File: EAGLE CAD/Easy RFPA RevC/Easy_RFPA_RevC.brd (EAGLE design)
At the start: 127 x 147.3 mm, 296 parts, among them IC1 LM741D, IC2 LM741D, IC3 LM393D, IC5 74AHC1G00DBV, IC6 74LS74D, IC7 74AHC1G86DBV, J401 HDR_2X1282836-1282836-1, J402 KK_PCFAN, Q1 IRF630, Q101 IRF520N, Q102 IRF630, Q2 MOSFET_NBSS123SOT23, Q201 IRF630, Q202 IRF630, Q3 NPNMMBT3904SOT23_BEC, Q301 MOSFET_NBSS123SOT23, Q302 PNPSOT23_BEC, Q303 NPNMMBT3904SOT23_BEC, Q4 PNPSOT23_BEC, Q5 IRF630, SW1 SPST_NO_TACT_RA43125608371643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, SW2 SPST_NO_TACT_RA43125608371643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, T1 HP1_TRAFO, T102 HP4_TRAFO, U1 OPAMP_QUADTLV274IDSOIC14, U2 ADJ_ZENERTL431AILPRAGTO-92-LP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, U302 OPAMP_QUADTLV274IDSOIC14, U401 LDO_3TERMMC78M12CTGTO220_VERT, U402 LDO_3TERMMC78M05CTGTO220_VERT, X1 1-227161-0, X2 1-227161-0, X4 1-227161-0, X402 HEATSINK_OMNI_DUALOMNI-UNI-30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

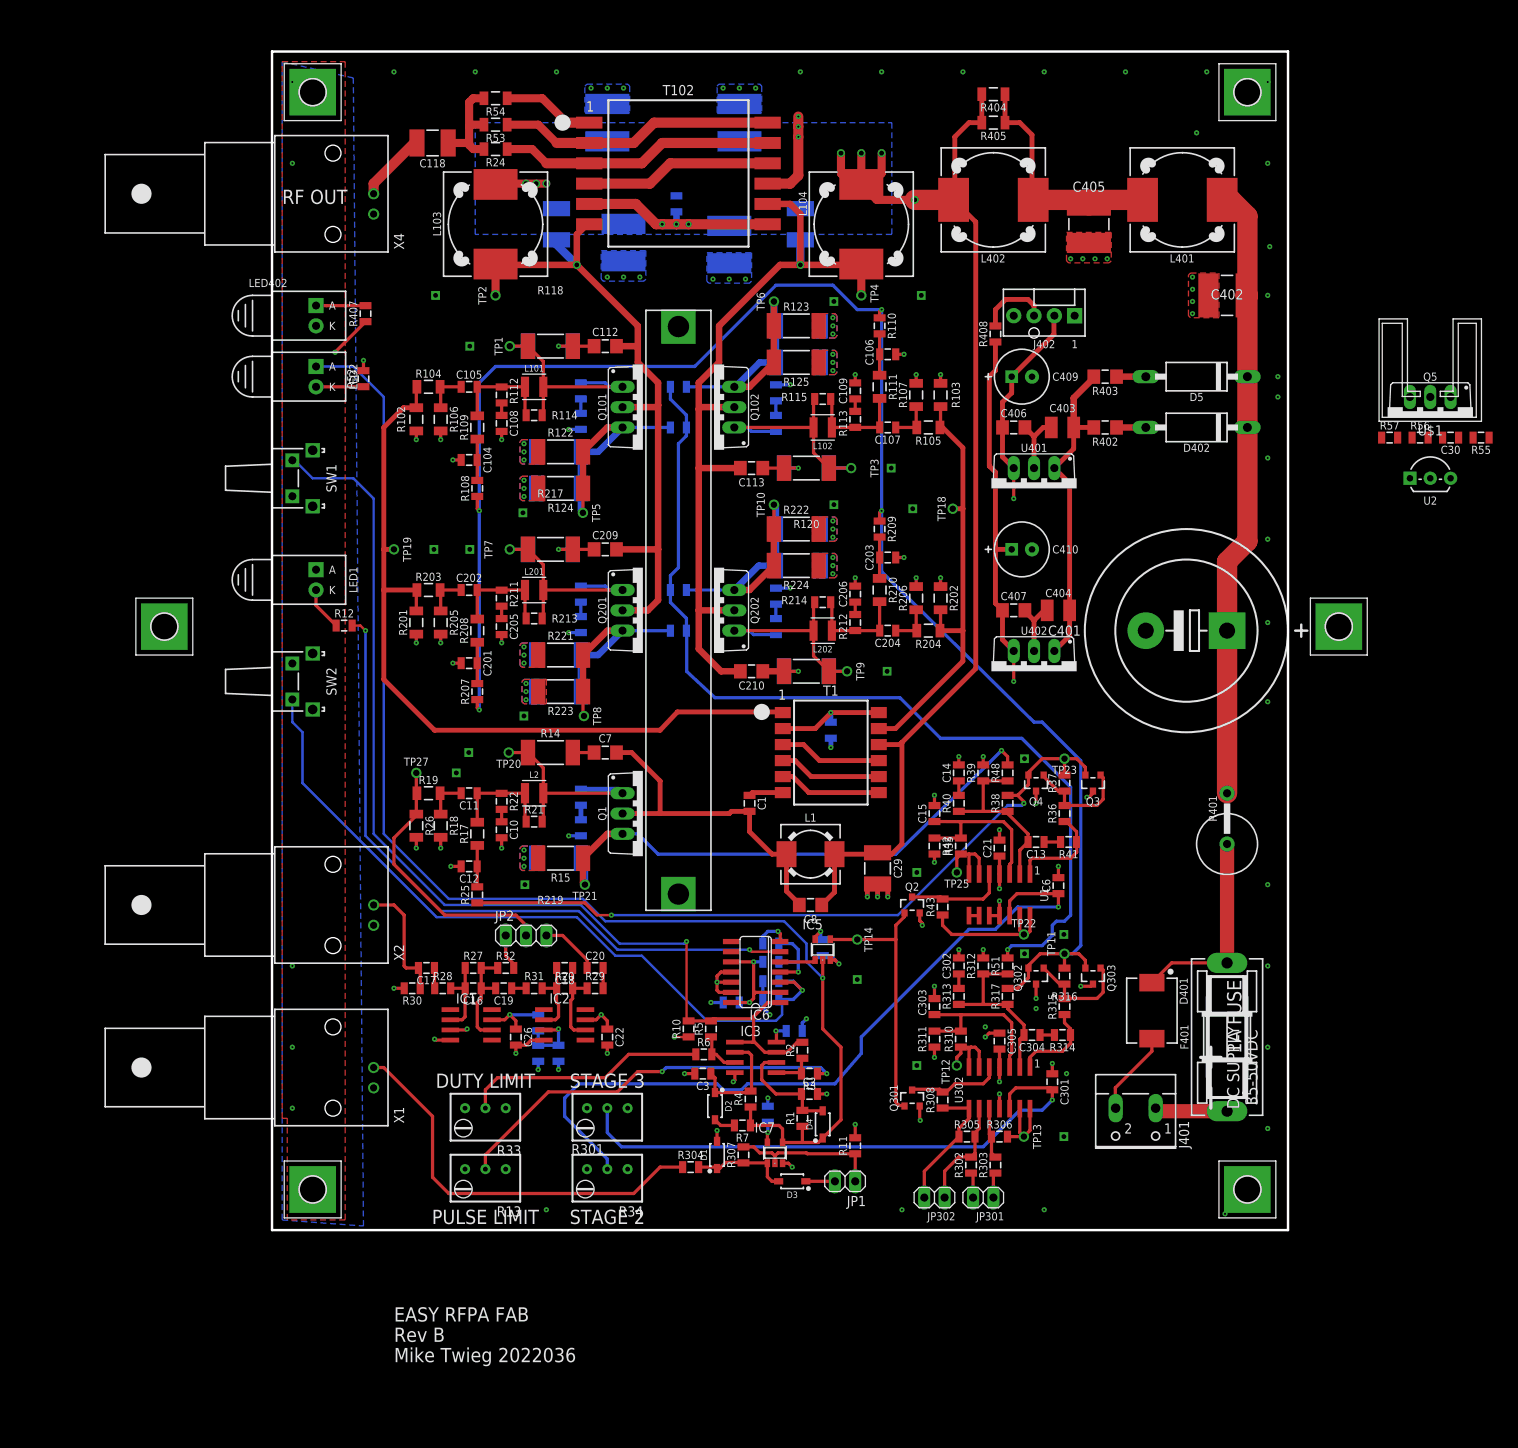
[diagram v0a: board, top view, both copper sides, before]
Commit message: Put discrete LDO on board
Remove old zeners
Move smaller electrolytic caps towards load circuitry to free up space
Move extra mounting holes onto board
Should consider reordering buttons/LEDs on west edge
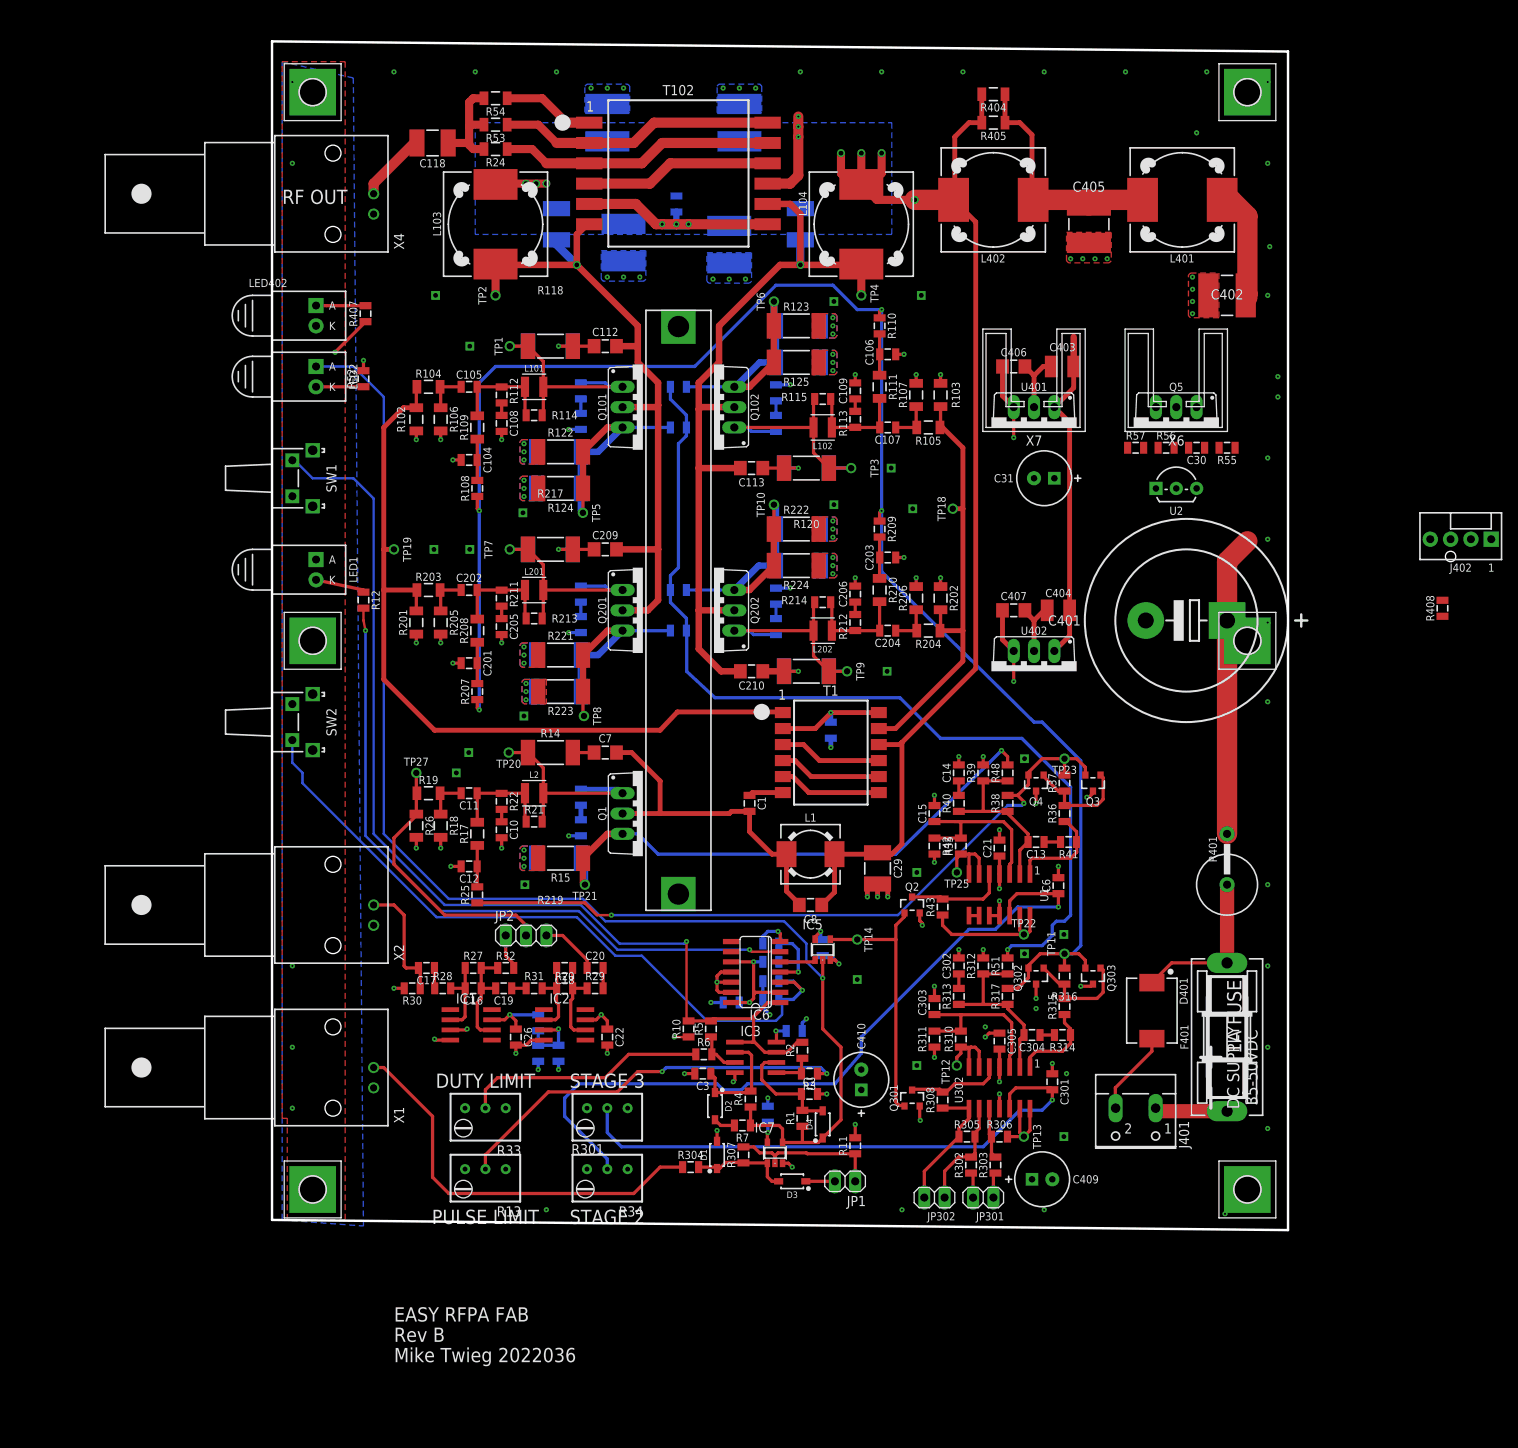
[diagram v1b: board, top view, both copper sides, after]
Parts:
- removed D402, D5: D-ZENER1N5355B-TPDO15-12, MDT_Diode:DO15-12
- removed R402, R403: 1.0, MDT_R:R1206
- removed U$1: (no value), MDT_HEATSINK:ATS-PCBT1085
- added C31: 22uF, MDT_C:E2,5-7
- added X6, X7: HEATSINK_CLIPONATS-PCBT1085ATS-PCBT1085, MDT_HEATSINK:ATS-PCBT1085
- moved C409 100.4 mm to (96.3, -1.27)
- moved C410 69.3 mm to (73.7, 11.2), turned to 90 degrees
- moved R408 65.6 mm to (146.3, 70.1)
- moved J402 59.1 mm to (148.6, 78.7)
- moved C30 31.8 mm to (115.6, 90.2)
- moved Q5 31.8 mm to (113.0, 92.7)
- moved R55 31.8 mm to (119.4, 90.2)
- moved U2 31.8 mm to (113.0, 85.1)
- moved R56 31.8 mm to (111.8, 90.2)
- moved R57 31.8 mm to (108.0, 90.2)
- moved H1 18.6 mm to (5.08, 66.0)
- moved H2 11.6 mm to (121.9, 66.0)
- moved C403 7.62 mm to (98.8, 100.3)
- moved C406 7.62 mm to (92.7, 100.3)
- moved U401 7.62 mm to (95.2, 92.7)
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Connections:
- removed net N$28: D5.A, R403.1
- removed net N$32: D402.A, R402.1
- net +24V: now also C31.+; no longer R402.2, R403.2
- net GND: now also C31.-
- net VB_ICL: no longer D402.C, D5.C
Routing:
- net VB_ICL: track 79.0 -> 52.0 mm
- net +5V: track 235.1 -> 208.4 mm
- net +12V: track 73.7 -> 61.8 mm
- net N$51: track 8.99 -> 0.00 mm
- net VB_FUSED: track 25.3 -> 20.2 mm
- net RESET: track 95.6 -> 90.5 mm
- net N$32: track 3.66 -> 0.00 mm
- net N$28: track 3.66 -> 0.00 mm
- net +24V: track 64.6 -> 65.8 mm
- net !READY: track 85.4 -> 86.3 mm
- net N$81: track 5.49 -> 6.33 mm
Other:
- board size 127 x 147.3 mm -> 127 x 148.6 mm

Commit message: TIP122 and angle bracket
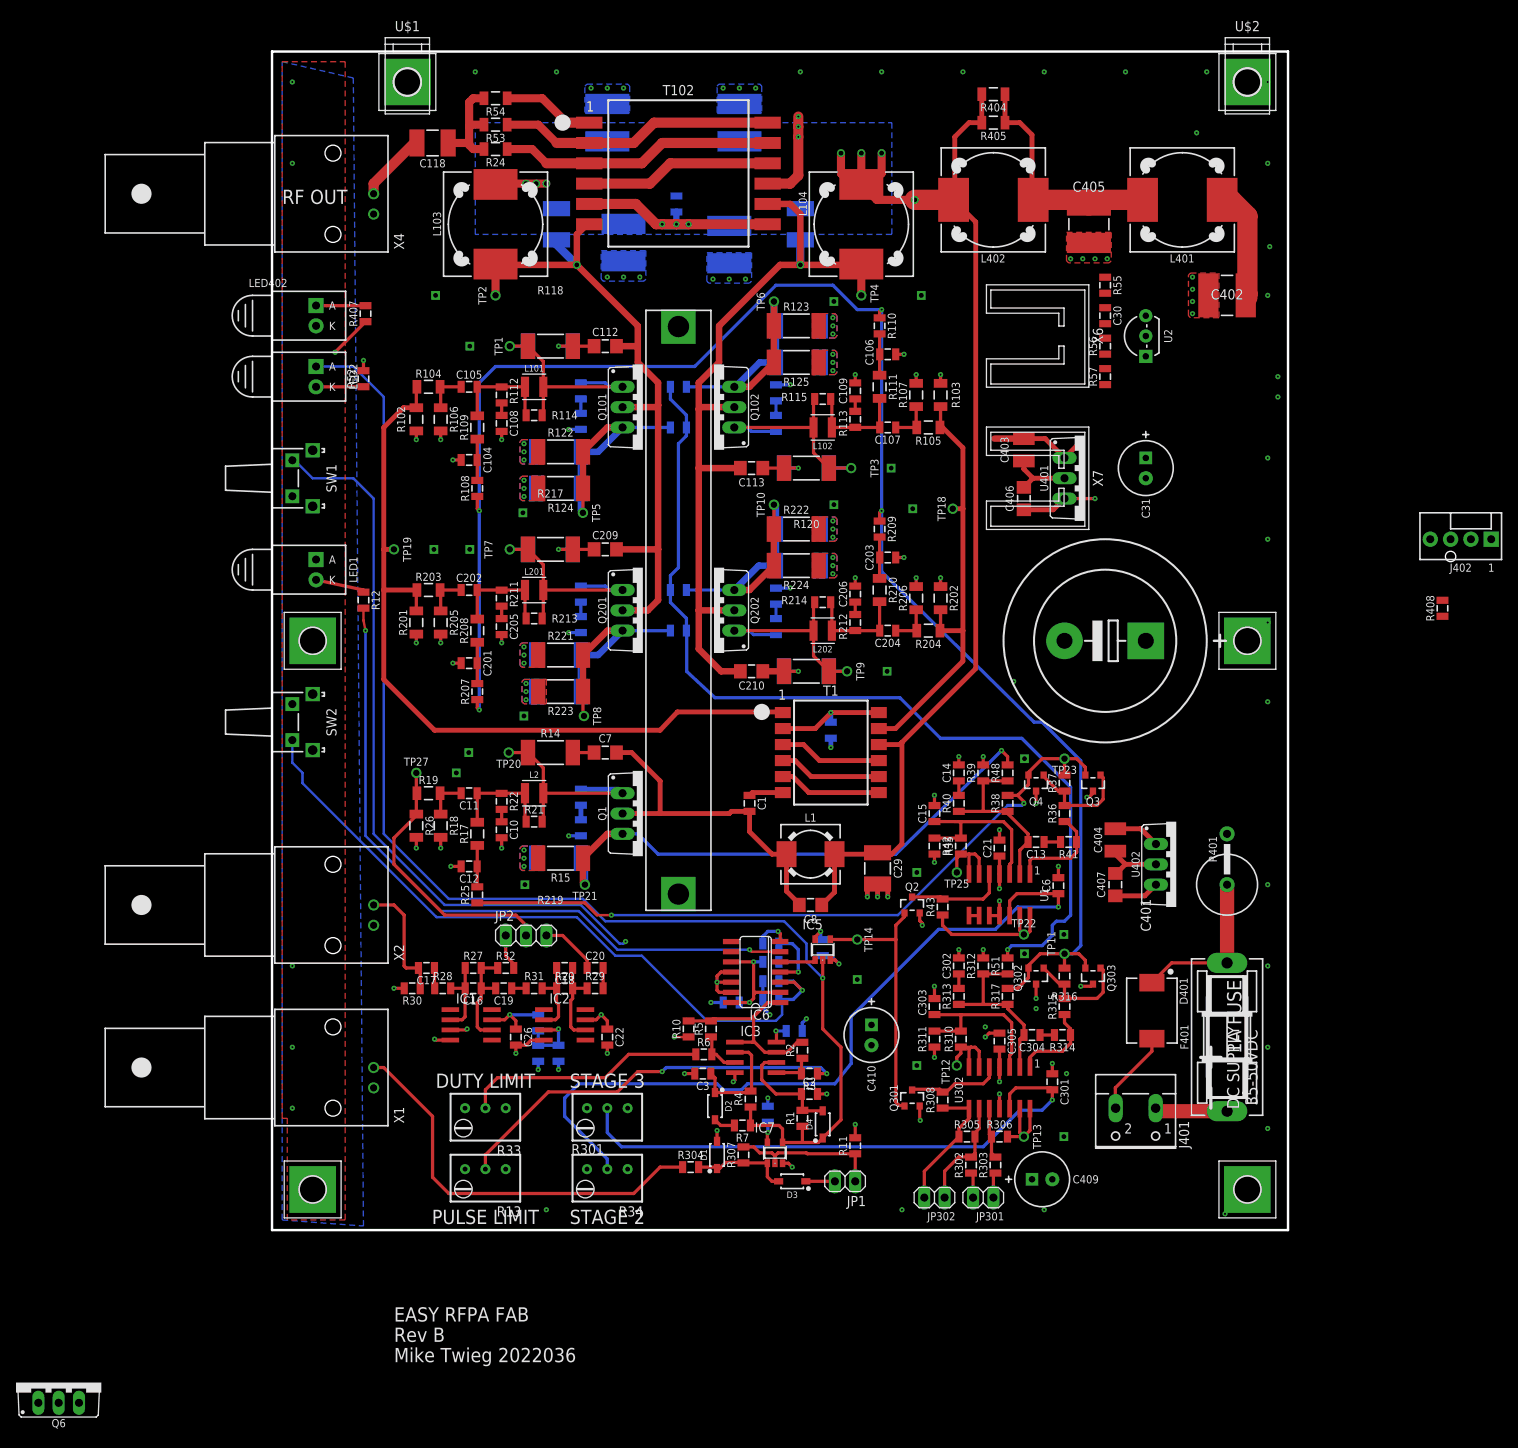
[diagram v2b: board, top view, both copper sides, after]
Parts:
- removed Q5: IRF630, MDT_TRANS:TO220BV
- added Q6: NPN_DARGLINGTONTIP122TO220BV, MDT_TRANS:TO220BV
- added U$1, U$2: (no value), MDT_HEATSINK:KEYSTONE_634
- moved C407 36.6 mm to (105.4, 35.6), turned to 90 degrees
- moved U402 30.0 mm to (113.0, 38.1), turned to 270 degrees
- moved C404 29.6 mm to (105.4, 41.1), turned to 270 degrees
- moved R55 25.4 mm to (104.1, 110.5), turned to 270 degrees
- moved C30 20.1 mm to (104.1, 106.7), turned to 270 degrees
- moved U2 19.4 mm to (109.2, 104.1), turned to 90 degrees
- moved C406 16.6 mm to (94.0, 83.8), turned to 90 degrees
- moved X6 16.2 mm to (101.6, 104.1), turned to 270 degrees
- moved R56 14.8 mm to (104.1, 102.9), turned to 90 degrees
- moved C31 12.8 mm to (109.2, 87.6), turned to 270 degrees
- moved H404 11.9 mm to (16.9, 135.9)
- moved C403 11.5 mm to (94.0, 89.9), turned to 270 degrees
- moved C401 10.5 mm to (104.1, 66.0)
- moved R57 9.67 mm to (104.1, 99.1), turned to 90 degrees
- moved U401 8.98 mm to (101.6, 86.4), turned to 270 degrees
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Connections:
- net +24V: now also Q6.S; no longer Q5.S
- net N$92: now also Q6.G; no longer Q5.G
- net VB_ICL: now also Q6.D; no longer Q5.D
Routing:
- net VB_ICL: track 52.0 -> 14.3 mm
- net +24V: track 65.8 -> 42.3 mm
- net !FAULT: track 133.9 -> 116.6 mm
- net +5V: track 208.4 -> 204.6 mm
- net N$64: track 94.7 -> 96.9 mm
- net +12V: track 61.8 -> 59.6 mm
- net GND: vias 153 -> 152
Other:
- board size 127 x 148.6 mm -> 127 x 147.3 mm
